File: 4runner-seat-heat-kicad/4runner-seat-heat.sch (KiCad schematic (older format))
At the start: 74 parts, among them J1 Toyota-90980-10964, J10 TE796864-3, J2 TE-284510-6, J3 TE-284539-6, J4 TE-796859-2, J5 Toyota-90980-10933, J6 TE-796859-2, J7 TE-284510-6, J8 TE-284539-6, J9 TE-796859-3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

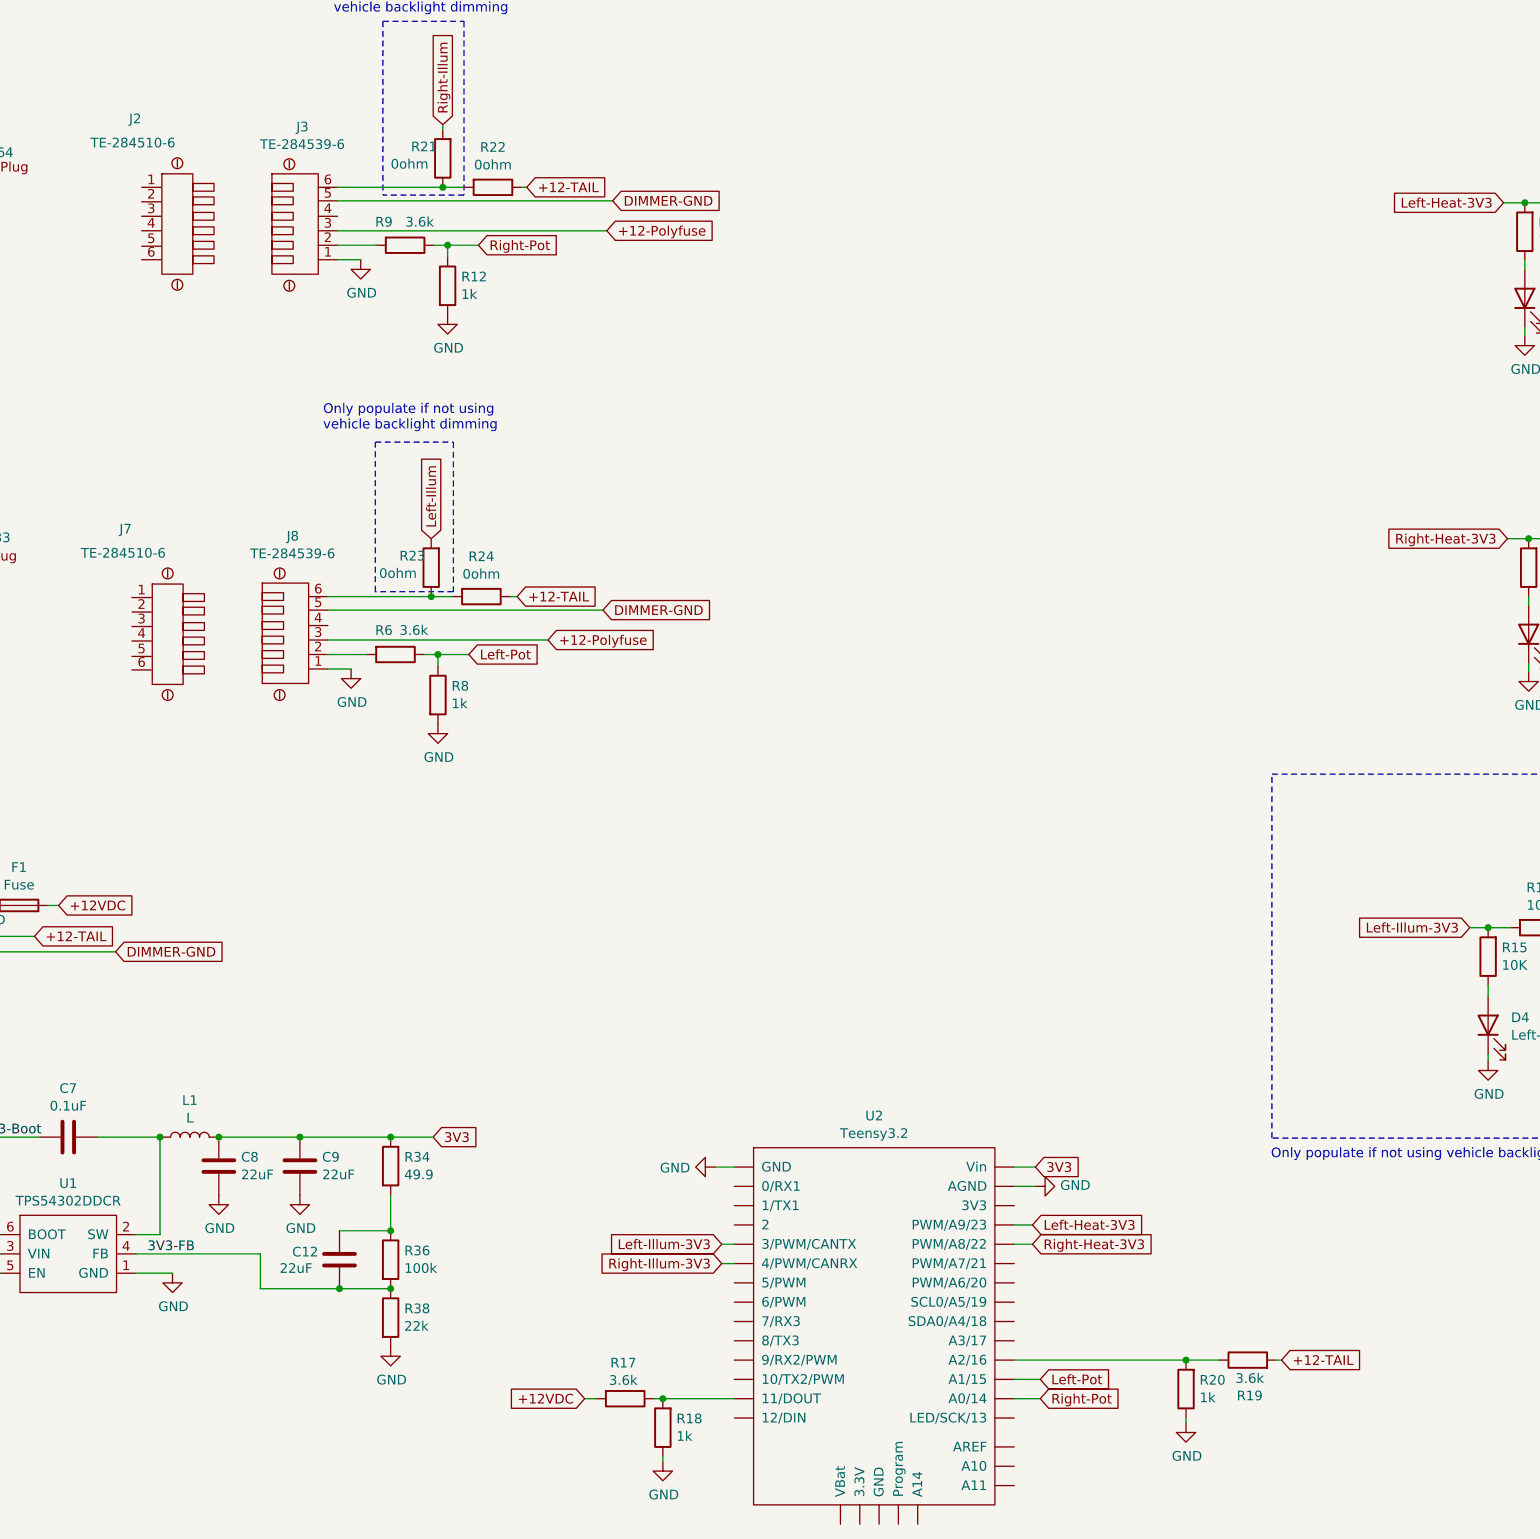
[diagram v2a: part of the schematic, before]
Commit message: silkscreen and small layout changes
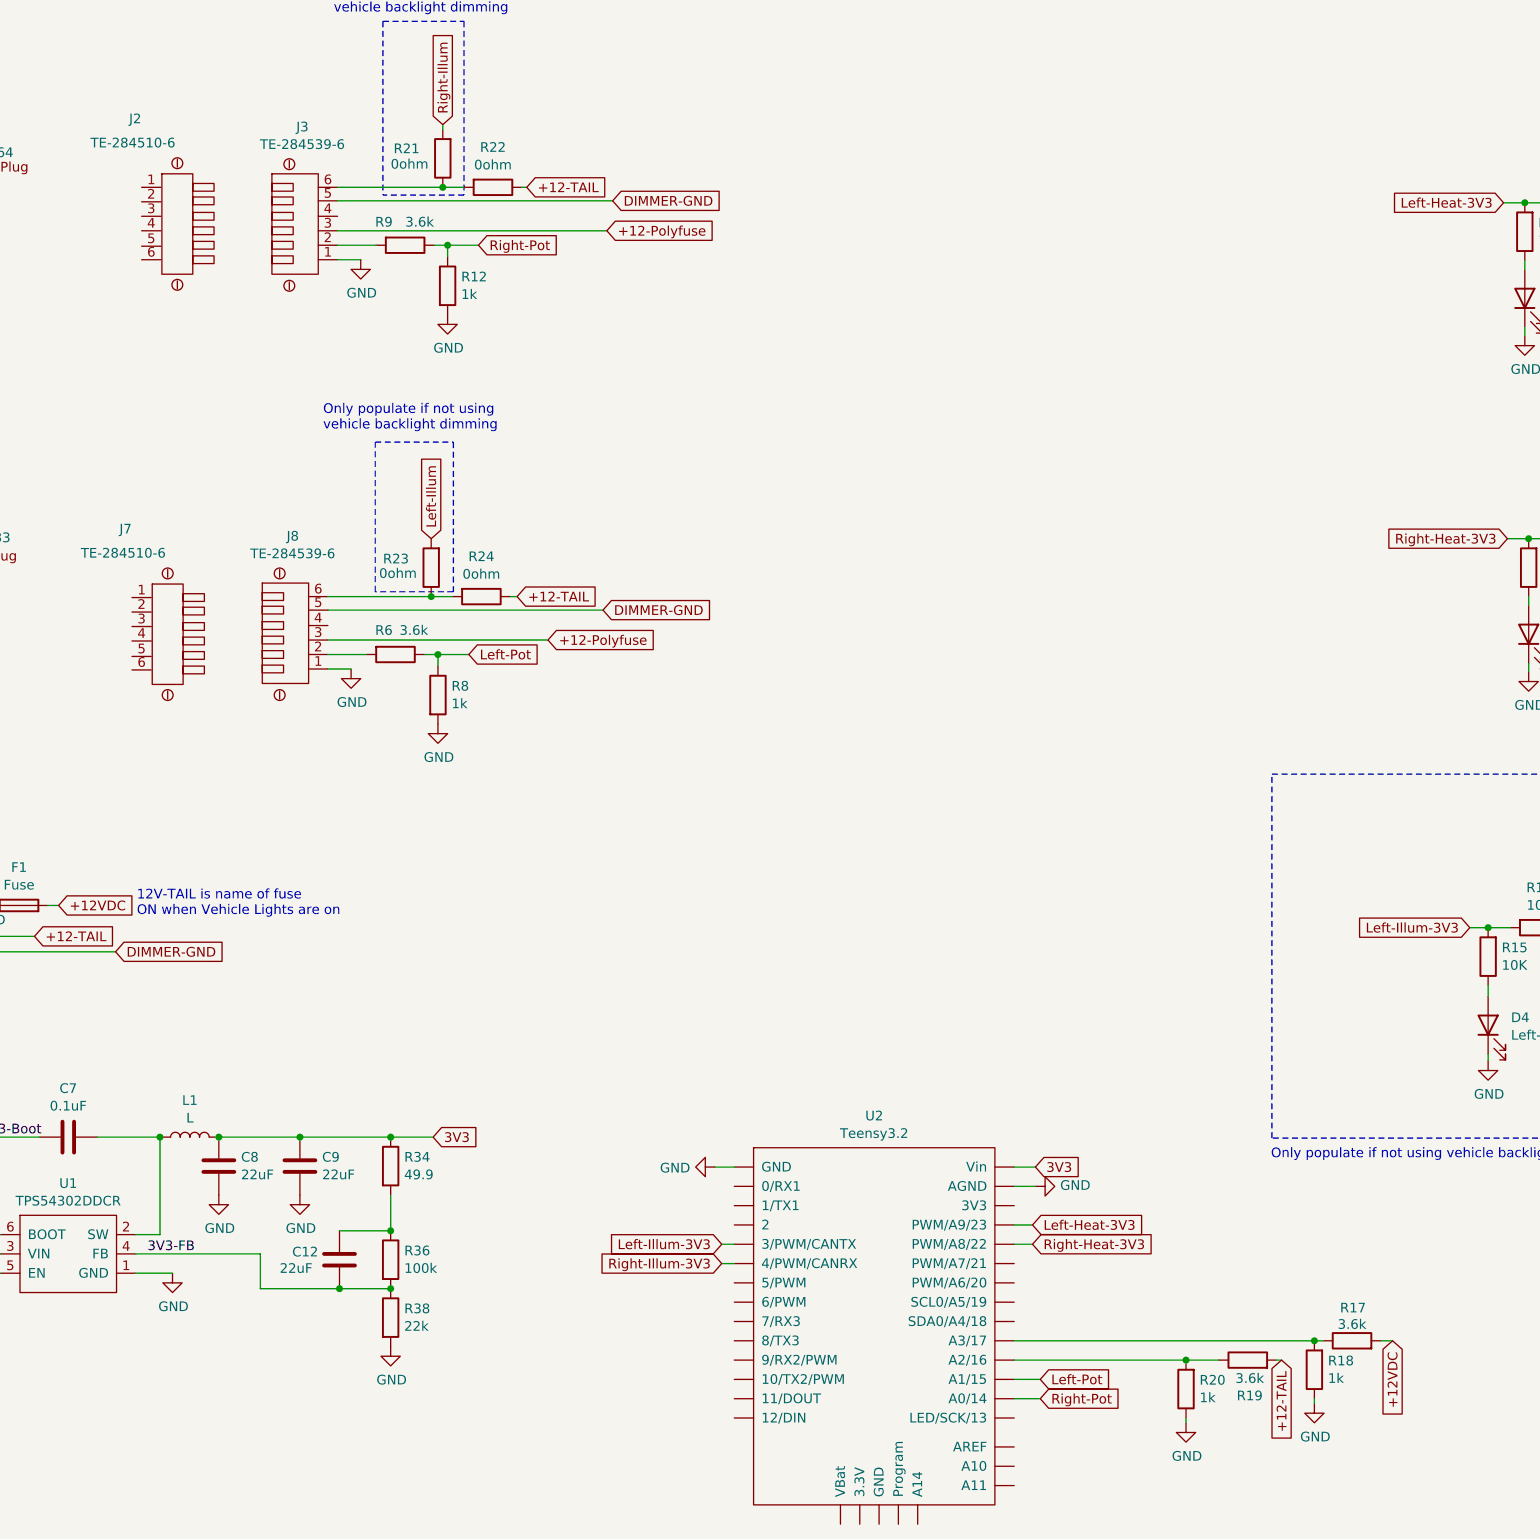
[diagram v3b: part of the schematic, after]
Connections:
- net at R17.1, R18.2: now also U2.17 (A3/17); no longer U2.11 (11/DOUT)
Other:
- note added: "12V-TAIL is name of fuse\nON when Vehicle Lights are on"
- moved on the sheet: R17, R18
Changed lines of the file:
@@
 	4810 6550 4815 6550
 Connection ~ 4810 6550
-Text GLabel 10620 7705 2    50   Input ~ 0
+Text GLabel 10620 7705 3    50   Input ~ 0
 +12-TAIL
 $Comp
@@
 U 1 1 6229FFBD
 P 6275 1480
-F 0 "R21" H 6440 1420 50  0000 R CNN
+F 0 "R21" H 6530 1430 50  0000 R CNN
 F 1 "0ohm" H 6545 1510 50  0000 R CNN
 F 2 "Resistor_SMD:R_0603_1608Metric" V 6205 1480 50  0001 C CNN
@@
 U 1 1 622E1A26
 P 6215 3600
-F 0 "R23" H 6380 3540 50  0000 R CNN
+F 0 "R23" H 6465 3555 50  0000 R CNN
 F 1 "0ohm" H 6485 3630 50  0000 R CNN
 F 2 "Resistor_SMD:R_0603_1608Metric" V 6145 3600 50  0001 C CNN
@@
 Text Notes 5710 735  0    50   ~ 0
 Only populate if not using \nvehicle backlight dimming
-Text GLabel 7010 7905 0    50   Input ~ 0
+Text GLabel 11195 7605 3    50   Input ~ 0
 +12VDC
 Wire Wire Line
-	7010 7905 7070 7905
+	11195 7605 11135 7605
 Wire Wire Line
-	7415 8205 7415 8230
+	10790 7905 10790 7930
 $Comp
 L power:GND #PWR023
 U 1 1 61D3CECA
-P 7415 8230
-F 0 "#PWR023" H 7415 7980 50  0001 C CNN
-F 1 "GND" H 7420 8057 50  0000 C CNN
-F 2 "" H 7415 8230 50  0001 C CNN
-F 3 "" H 7415 8230 50  0001 C CNN
-	1    7415 8230
+P 10790 7930
+F 0 "#PWR023" H 10790 7680 50  0001 C CNN
+F 1 "GND" H 10795 7757 50  0000 C CNN
+F 2 "" H 10790 7930 50  0001 C CNN
+F 3 "" H 10790 7930 50  0001 C CNN
+	1    10790 7930
 	1    0    0    -1
+$EndComp
+Text Notes 4690 5410 0    50   ~ 0
+12V-TAIL is name of fuse\nON when Vehicle Lights are on
+$Comp
+L Device:R R18
+U 1 1 61D3C8DB
+P 10790 7755
+F 0 "R18" H 10720 7709 50  0000 R CNN
+F 1 "1k" H 10720 7800 50  0000 R CNN
+F 2 "Resistor_SMD:R_0603_1608Metric" V 10720 7755 50  0001 C CNN
+F 3 "~" H 10790 7755 50  0001 C CNN
+	1    10790 7755
+	-1   0    0    1
 $EndComp
 $Comp
 L Device:R R17
 U 1 1 61D3CEBE
-P 7220 7905
-F 0 "R17" V 7035 7895 50  0000 C CNN
-F 1 "3.6k" V 7125 7895 50  0000 C CNN
-F 2 "Resistor_SMD:R_0603_1608Metric" V 7150 7905 50  0001 C CNN
-F 3 "~" H 7220 7905 50  0001 C CNN
-	1    7220 7905
-	0    1    1    0
+P 10985 7605
+F 0 "R17" V 11155 7600 50  0000 C CNN
+F 1 "3.6k" V 11070 7605 50  0000 C CNN
+F 2 "Resistor_SMD:R_0603_1608Metric" V 10915 7605 50  0001 C CNN
+F 3 "~" H 10985 7605 50  0001 C CNN
+	1    10985 7605
+	0    -1   -1   0
 $EndComp
-$Comp
-L Device:R R18
-U 1 1 61D3C8DB
-P 7415 8055
-F 0 "R18" H 7345 8009 50  0000 R CNN
-F 1 "1k" H 7345 8100 50  0000 R CNN
-F 2 "Resistor_SMD:R_0603_1608Metric" V 7345 8055 50  0001 C CNN
-F 3 "~" H 7415 8055 50  0001 C CNN
-	1    7415 8055
-	-1   0    0    1
-$EndComp
+Connection ~ 10790 7605
 Wire Wire Line
-	7415 7905 7370 7905
-Connection ~ 7415 7905
+	10790 7605 10835 7605
 Wire Wire Line
-	7785 7905 7415 7905
+	9235 7605 10790 7605
 $EndSCHEMATC

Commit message: push all versions to rev03
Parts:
- J10: footprint _4runner-seat-heat-custom-libraries:TE-796864-3 -> _4runner-seat-heat-custom-libraries:TE-796864-4
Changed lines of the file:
@@
 F 0 "J10" H 3063 5403 50  0000 C CNN
 F 1 "TE796864-3" H 3063 5312 50  0000 C CNN
-F 2 "_4runner-seat-heat-custom-libraries:TE-796864-3" H 3025 5300 50  0001 C CNN
+F 2 "_4runner-seat-heat-custom-libraries:TE-796864-4" H 3025 5300 50  0001 C CNN
 F 3 "" H 3025 5300 50  0001 C CNN
 	1    2995 5210
